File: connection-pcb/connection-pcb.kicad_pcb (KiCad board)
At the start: 2 copper layers, 19 parts, among them J1 Conn_01x05, J2 Conn_01x05, J3 Conn_01x05, J4 Conn_01x05, J5 Conn_01x05, J6 Screw_Terminal_01x04, J7 Screw_Terminal_01x02, J8 Screw_Terminal_01x06, J9 DE9_Socket_MountingHoles, SW1 SW_DIP_x04

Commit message: Finish routing
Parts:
- moved J7 113.8 mm to (56.5, 27.8), turned to 180 degrees
- moved J9 106.4 mm to (42.7, 46.3), turned to -90 degrees
- moved TP6 104.0 mm to (55.2, 39.5)
- moved TP5 97.0 mm to (55.2, 47.2)
- moved TP1 90.5 mm to (69.5, 27.8)
- moved TP2 89.5 mm to (77.5, 27.8)
- moved TP4 87.8 mm to (85.5, 27.8)
- moved TP3 79.3 mm to (93.5, 27.8)
- moved R3 73.7 mm to (144.2, 33.4), turned to -90 degrees
- moved R2 65.9 mm to (137.3, 34.0), turned to 180 degrees
- moved J6 65.2 mm to (111.5, 27.8), turned to 180 degrees
- moved SW1 50.9 mm to (129.7, 47.1), turned to 90 degrees
- moved J1 48.5 mm to (65.2, 49.5), turned to 90 degrees
- moved R1 39.3 mm to (122.0, 52.0)
- moved J8 38.9 mm to (153.2, 40.8), turned to 90 degrees
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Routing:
- net /CAN_L: track 0.00 -> 144.2 mm, vias 0 -> 2
- net /CAN_H: track 0.00 -> 141.6 mm
- net /PCAN_+5V: track 0.00 -> 115.0 mm
- net +24V: track 0.00 -> 98.0 mm
- net +12V: track 0.00 -> 42.8 mm
- net /N_WAKEUP: track 0.00 -> 27.7 mm
- net Net-(R2-Pad1): track 0.00 -> 5.45 mm
- net Net-(R1-Pad2): track 0.00 -> 4.96 mm
- added copper zone on B.Cu, net +12V
- added copper zone on B.Cu, net +5V
- added copper zone on F.Cu, net GND
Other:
- board outline added: 126.5 x 36.5 mm
- board text added: "+12V"
- board text added: "+24V"
- board text added: "+5V"
- board text added: "120"
- board text added: "120R_H"
- board text added: "120R_L"
- board text added: "22k"
- board text added: "CAN_H"
- board text added: "CAN_L"
- board text added: "DC-DC"
- board text added: "GND"
- board text added: "N_WU"
- board text added: "PCAN"
- board text added: "PCAN_5"

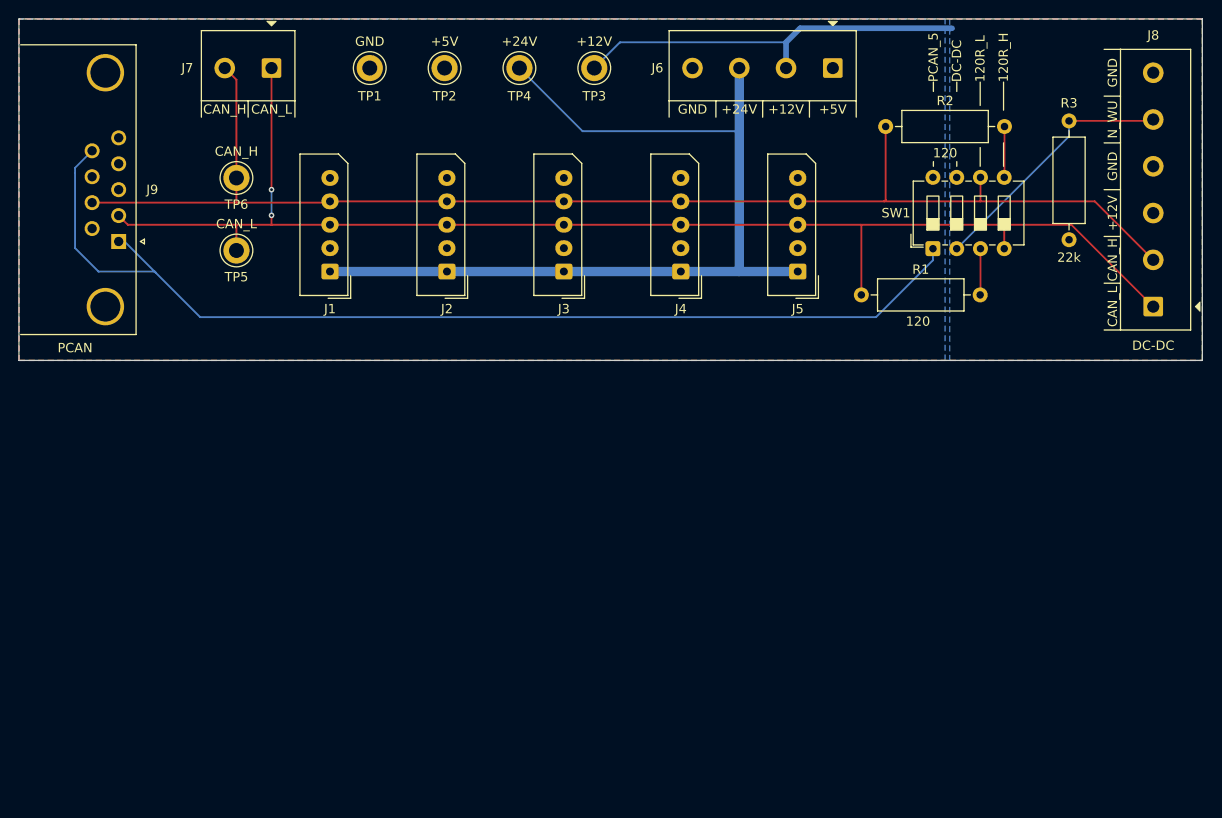
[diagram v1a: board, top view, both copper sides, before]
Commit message: Add mounting holes
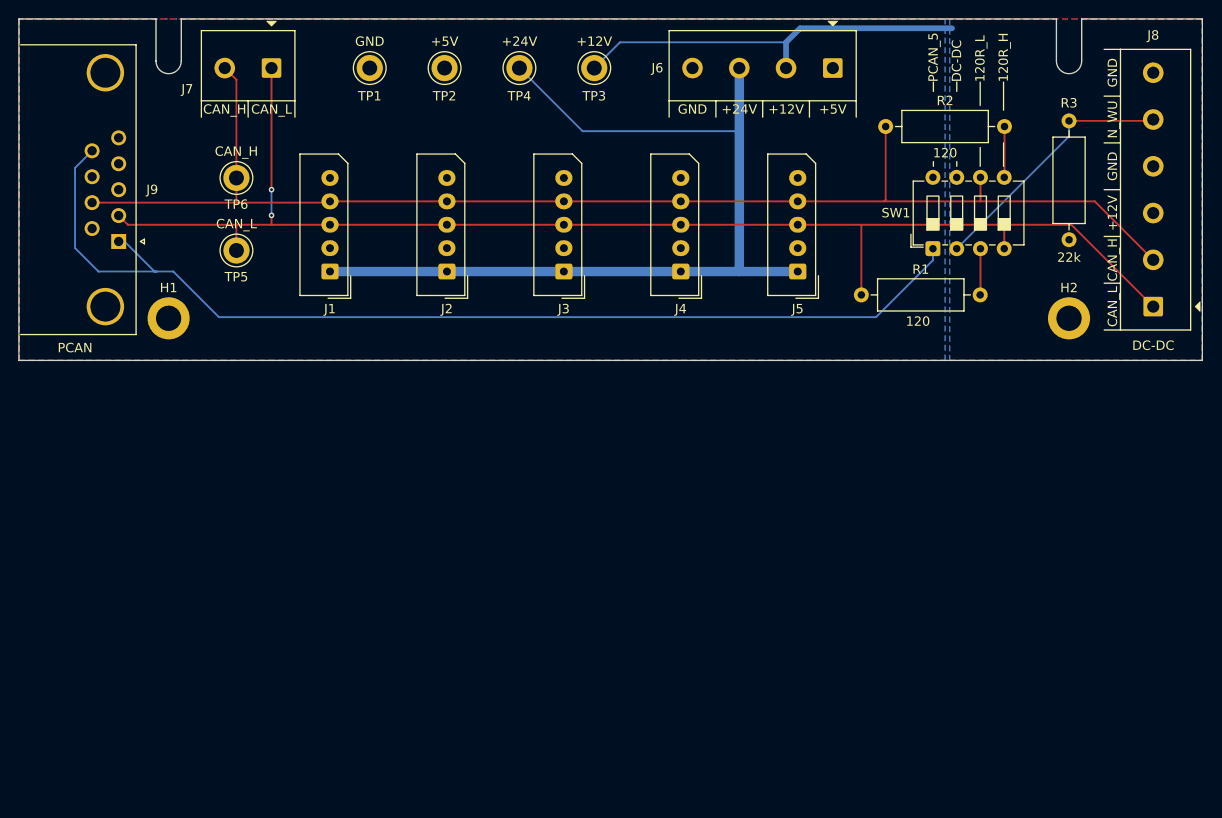
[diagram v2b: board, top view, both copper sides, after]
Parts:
- added H1: MountingHole_Pad, MountingHole:MountingHole_2.7mm_M2.5_ISO7380_Pad, F.Cu at (48.0, 54.5)
- added H2: MountingHole_Pad, MountingHole:MountingHole_2.7mm_M2.5_ISO7380_Pad, F.Cu at (144.2, 54.5)
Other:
- outline, holes or cut-outs redrawn

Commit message: Fix unconnected trace
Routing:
- net /PCAN_+5V: track 115.1 -> 116.8 mm
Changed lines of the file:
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@@
+	)
+	(segment
+		(start 42.660331 46.29)
+		(end 45.29 46.29)
+		(width 0.2)
+		(layer "B.Cu")
+		(net 10)
 	)
 	(segment
@@
 	)
 	(segment
-		(start 38 38.415331)
-		(end 38 39)
+		(start 45.29 46.29)
+		(end 48.5 49.5)
 		(width 0.2)
 		(layer "B.Cu")
@@
 	)
 	(segment
-		(start 46.5 49.5)
-		(end 48.5 49.5)
+		(start 53.375 54.375)
+		(end 123.625 54.375)
 		(width 0.2)
 		(layer "B.Cu")
@@
 	)
 	(segment
-		(start 38 39)
-		(end 38 47)
-		(width 0.2)
-		(layer "B.Cu")
-		(net 10)
-	)
-	(segment
-		(start 53.375 54.375)
-		(end 123.625 54.375)
-		(width 0.2)
-		(layer "B.Cu")
-		(net 10)
-	)
-	(segment
-		(start 46.75 49.5)
-		(end 46.5 49.5)
-		(width 0.2)
-		(layer "B.Cu")
-		(net 10)
-	)
-	(segment
 		(start 48.5 49.5)
 		(end 53.375 54.375)
@@
 	)
 	(segment
-		(start 46.5 49.5)
-		(end 43.29 46.29)
+		(start 40.5 49.5)
+		(end 48.5 49.5)
 		(width 0.2)
 		(layer "B.Cu")
@@
 	)
 	(segment
-		(start 43.29 46.29)
-		(end 42.660331 46.29)
+		(start 38 38.415331)
+		(end 38 47)
 		(width 0.2)
 		(layer "B.Cu")
-		(net 10)
-	)
-	(segment
-		(start 40.5 49.5)
-		(end 46.5 49.5)
-		(width 0.2)
-		(layer "B.Cu")
